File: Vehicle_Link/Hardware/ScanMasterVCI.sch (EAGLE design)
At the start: 96 parts, among them IC1 XMEGA32A4U, IC2 TL331, IC3 TL331, IC4 TL331, IC5 TL331, Q1 MMBT4403, Q10 ZXMP6A17G, Q2 MMBT3904, Q3 RUM002N05, Q5 RUM002N05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

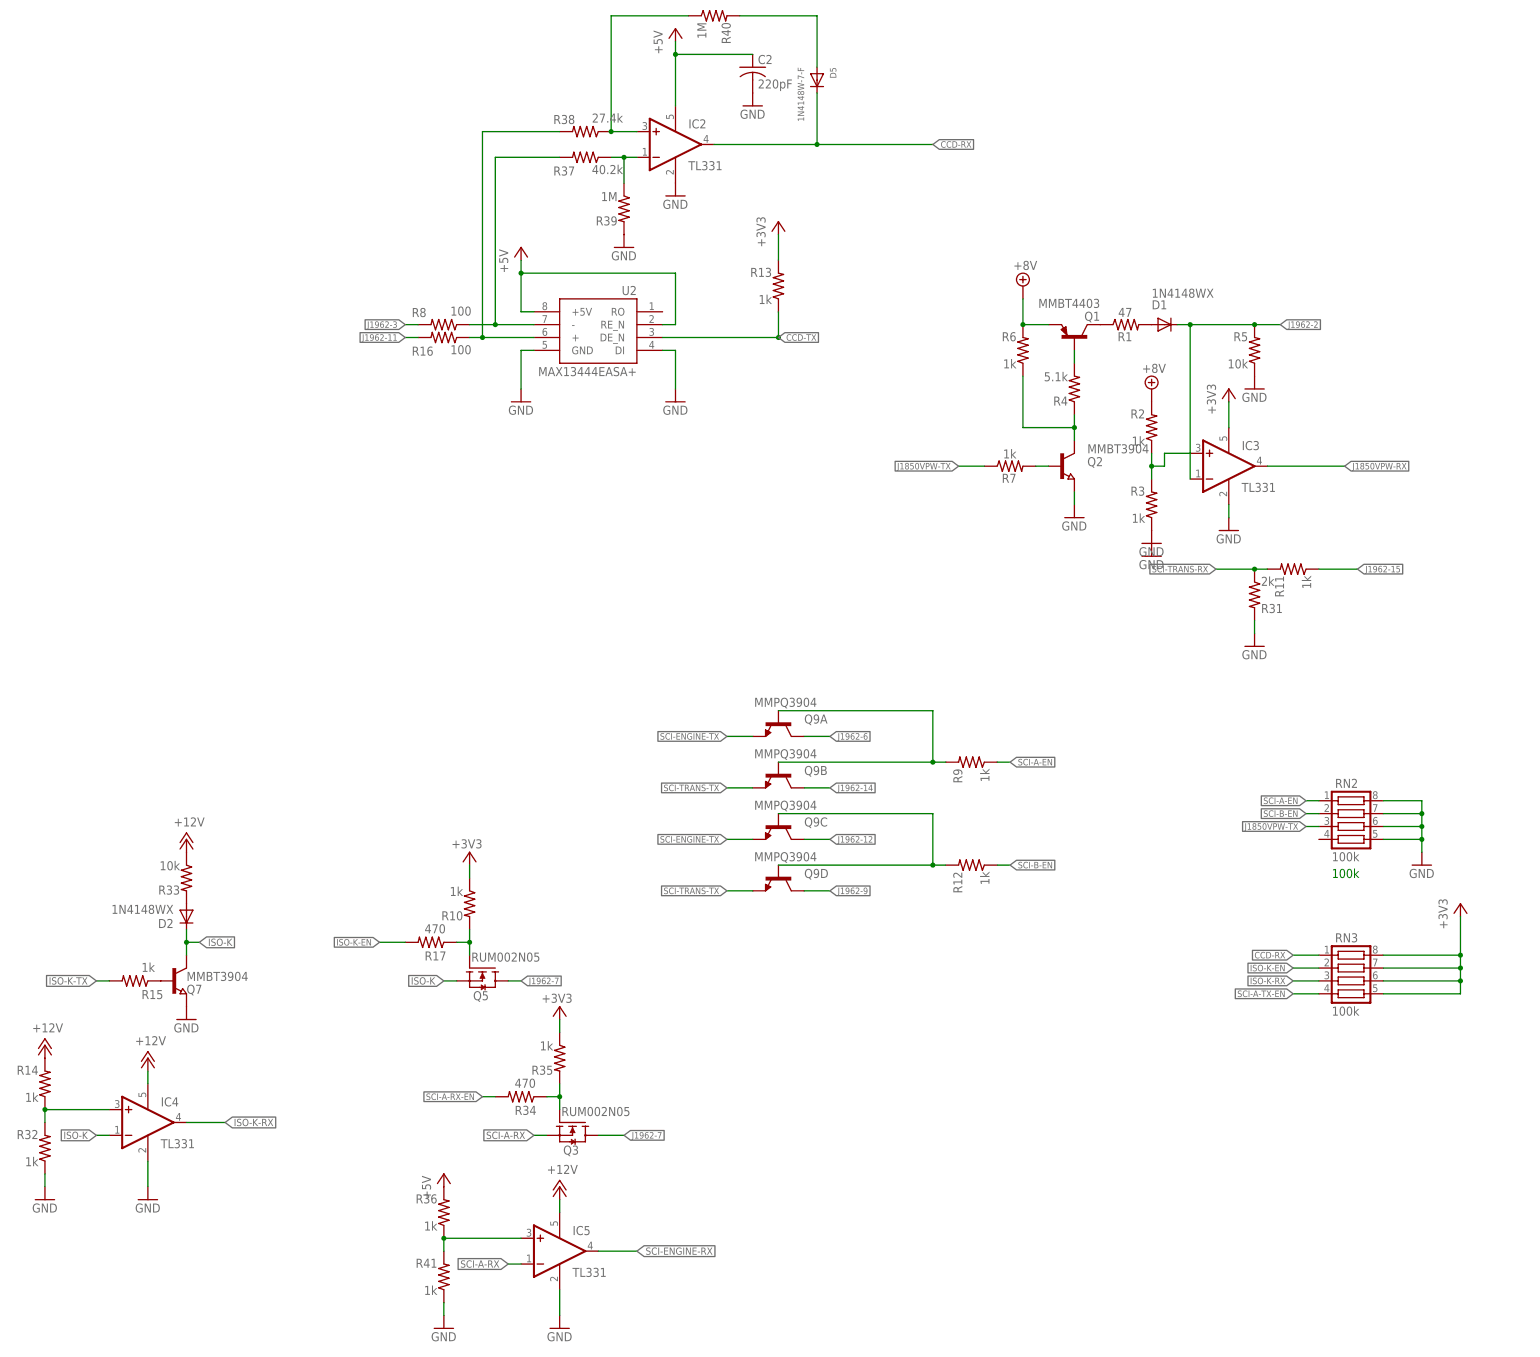
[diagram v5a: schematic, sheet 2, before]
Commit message: Removed the BJTs I was using. Going to try the schematic with MOSFETs.
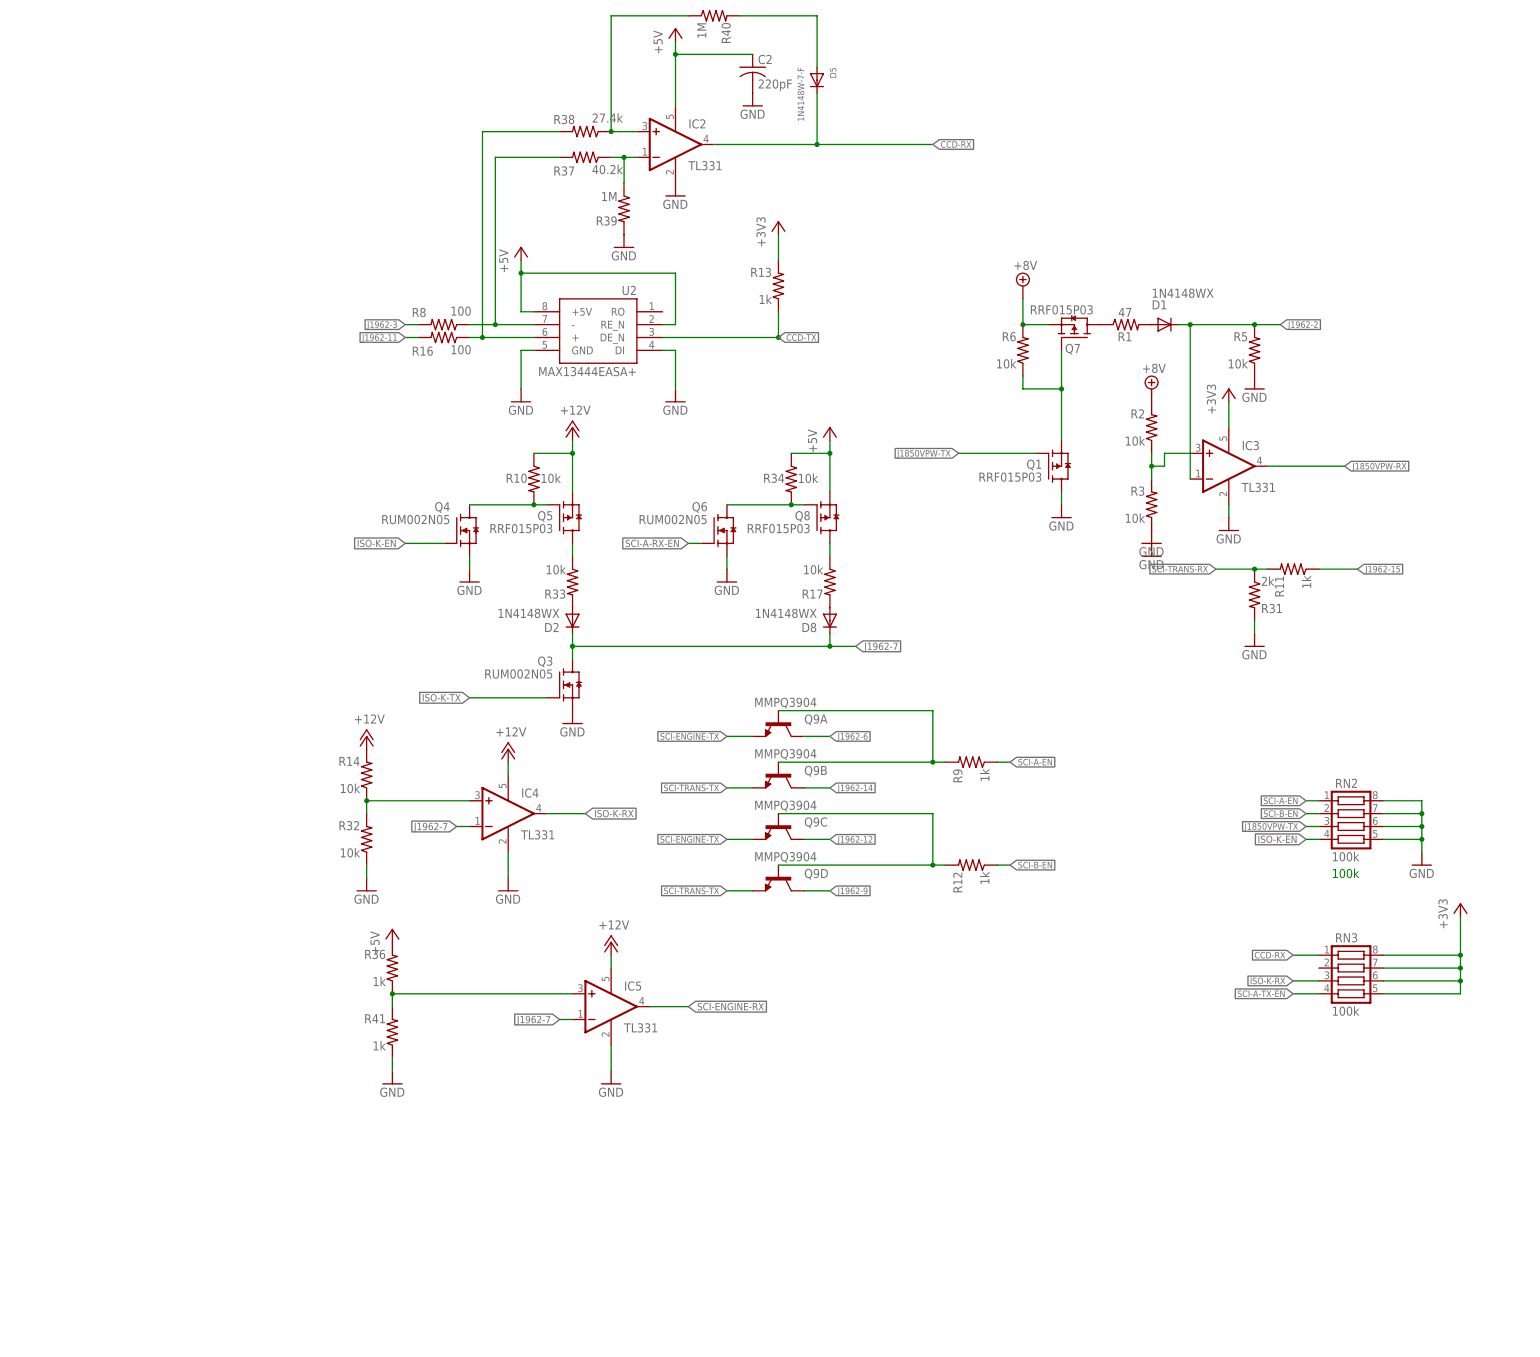
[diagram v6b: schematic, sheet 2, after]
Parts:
- removed Q2: MMBT3904, semicon-smd-ipc:NPN-TRANSISTOR_SOT23
- removed R15, R35, R7: 1k, adafruit:R-US_R0603
- removed R4: 5.1k, adafruit:R-US_R0603
- added D8: 1N4148WX, diode:DIODE-SOD323-R
- added Q4, Q6: RUM002N05, customics:RUM002N05
- added Q8: RRF015P03, customics:RRF015P03
- Q1: value MMBT4403 -> RRF015P03; device transistor-pnp:MMBT4403LT1SMD -> customics:RRF015P03
- Q5: value RUM002N05 -> RRF015P03; device customics:RUM002N05 -> customics:RRF015P03
- Q7: value MMBT3904 -> RRF015P03; device semicon-smd-ipc:NPN-TRANSISTOR_SOT23 -> customics:RRF015P03
- R10, R14, R2, R3, R32, R6: value 1k -> 10k
- R17, R34: value 470 -> 10k
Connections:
- removed net ISO-K: D2.C, IC4.-IN, Q5.S, Q7.C
- removed net N$13: Q7.B, R15.1
- removed net N$28: Q1.B, R4.2
- removed net N$29: Q1.C, R1.1
- removed net N$6: Q2.B, R7.2
- removed net SCI-A-RX: IC5.-IN, Q3.S
- new net N$21: D8.A, R17.2
- new net N$22: Q5.D, R33.1
- new net N$23: Q6.D, Q8.G, R34.2
- new net N$31: Q8.D, R17.1
- net +12V: now also Q5.S, R10.1; no longer R33.1
- net +3V3: no longer R10.1, R35.1
- net +5V: now also Q8.S, R34.1
- net +8V: now also Q7.S; no longer Q1.E
- net GND: now also Q1.D, Q3.S, Q4.S, Q6.S; no longer Q2.E, Q7.E
- net ISO-K-EN: now also Q4.G, RN2.4; no longer R17.2, RN3.2
- net ISO-K-TX: now also Q3.G; no longer R15.2
- net J1850VPW-TX: now also Q1.G; no longer R7.1
- net J1962-7: now also D2.C, D8.C, IC4.-IN, IC5.-IN; no longer Q5.D
- net N$10: now also Q7.D, R1.1; no longer Q3.G, R34.1, R35.2
- net N$26: now also Q1.S, Q7.G; no longer Q2.C, R4.1
- net N$4: now also Q4.D; no longer R17.1
- net SCI-A-RX-EN: now also Q6.G; no longer R34.2
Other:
- moved on the sheet: D2, IC4, IC5, Q3, R10, R14, R17, R32, R33, R34, R36, R41

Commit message: Last set of commits for redesigning comm circuits (hopefully). I've tested all the circuits individually. Added the new connector for the OBD -> board connection.
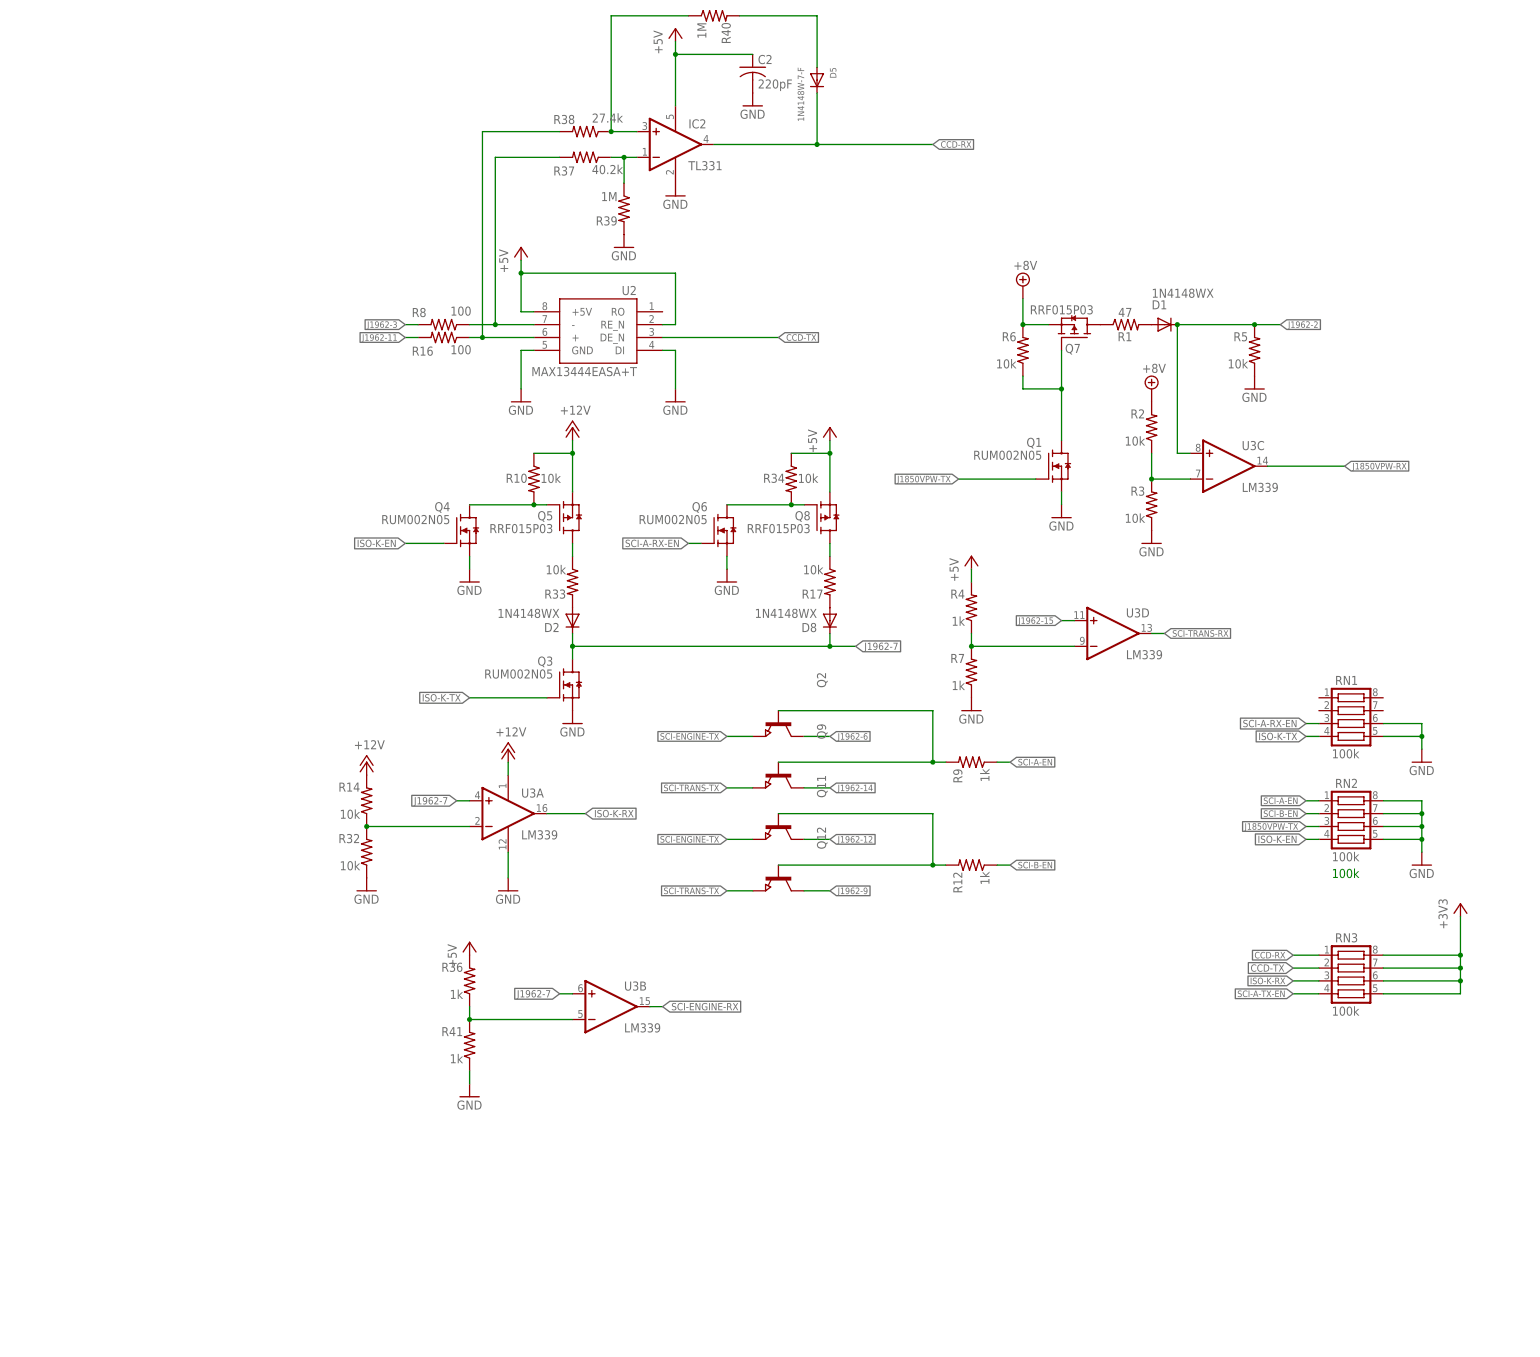
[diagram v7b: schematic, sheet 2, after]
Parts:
- removed IC3, IC4, IC5: TL331, linear:TL331
- removed P11, P12, P14, P15, P16, P2, P3, P4, P6, P7, P9: (no value), pinhead:PINHD-1X1
- removed R11, R13: 1k, adafruit:R-US_R0603
- removed R31: 2k, adafruit:R-US_R0603
- added C1, C3, C4: 100nF, adafruit:C-USC0402
- added P1: HARFLEX-1515012-601, customics:HARFLEX-1515012-601
- added Q11, Q12, Q2: (no value), semicon-smd-ipc:NPN-TRANSISTOR_SOT23
- added R4, R7: 1k, adafruit:R-US_R0603
- added RN1: 100k, resistor-net:CTS742C083
- added U3: LM339, customics:LM339
- D6: value 1.5SMC43AT3G -> 1.5SMC43AT3G
- Q1: value RRF015P03 -> RUM002N05; device customics:RRF015P03 -> customics:RUM002N05
- Q9: value MMPQ3904 -> (none); device customics:MMPQ3904 -> semicon-smd-ipc:NPN-TRANSISTOR_SOT23
- U1: value L78L08ABUTR -> L78L
- U2: value MAX13444EASA+ -> MAX13444EASA+T
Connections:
- new net N$6: R4.1, R7.2, U3D.-IN
- net +12V: now also U1.VIN, U3A.V+; no longer IC4.V+, IC5.V+, U1.VOUT
- net +3V3: now also C1.1, C3.1, C4.1; no longer IC3.V+, R13.2
- net +5V: now also R4.2
- net +8V: now also U1.VOUT; no longer U1.VIN
- net CCD-TX: now also RN3.2; no longer R13.1
- net GND: now also C1.2, C3.2, C4.2, P1.6, Q1.S, R7.1, RN1.5, RN1.6, U3A.V-; no longer IC3.GND, IC4.GND, IC5.GND, P4.1, Q1.D, R31.2
- net ISO-K-RX: now also U3A.OUT; no longer IC4.OUT
- net ISO-K-TX: now also RN1.4
- net J1850VPW-RX: now also U3C.OUT; no longer IC3.OUT
- net J1962-11: now also P1.10; no longer P11.1
- net J1962-12: now also P1.9, Q11.C; no longer P12.1, Q9C.C
- net J1962-14: now also P1.4, Q9.C; no longer P14.1, Q9B.C
- net J1962-15: now also P1.2, U3D.+IN; no longer P15.1, R11.1
- net J1962-16: now also P1.7; no longer P16.1
- net J1962-2: now also P1.1, U3C.+IN; no longer IC3.-IN, P2.1
- net J1962-3: now also P1.11; no longer P3.1
- net J1962-6: now also P1.5, Q2.C; no longer P6.1, Q9A.C
- net J1962-7: now also P1.3, U3A.+IN, U3B.+IN; no longer IC4.-IN, IC5.-IN, P7.1
- net J1962-9: now also P1.8, Q12.C; no longer P9.1, Q9D.C
- net N$1: now also Q2.B, Q9.B; no longer Q9A.B, Q9B.B
- net N$14: now also U3B.-IN; no longer IC5.+IN
- net N$26: now also Q1.D; no longer Q1.S
- net N$37: now also U3C.-IN; no longer IC3.+IN
- net N$5: now also Q11.B, Q12.B; no longer Q9C.B, Q9D.B
- net N$8: now also U3A.-IN; no longer IC4.+IN
- net SCI-A-RX-EN: now also RN1.3
- net SCI-ENGINE-RX: now also U3B.OUT; no longer IC5.OUT
- net SCI-ENGINE-TX: now also Q11.E, Q2.E; no longer Q9A.E, Q9C.E
- net SCI-TRANS-RX: now also U3D.OUT; no longer R11.2, R31.1
- net SCI-TRANS-TX: now also Q12.E, Q9.E; no longer Q9B.E, Q9D.E
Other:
- moved on the sheet: R14, R32, R36, R41
